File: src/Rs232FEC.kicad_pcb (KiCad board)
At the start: 2 copper layers, 24 x 27.9 mm, 26 parts, among them J1 B5B-XH-A, P1 105444-0001, Q1 DMP3099L-13, U1 FT232RL, U2 MAX232IDR

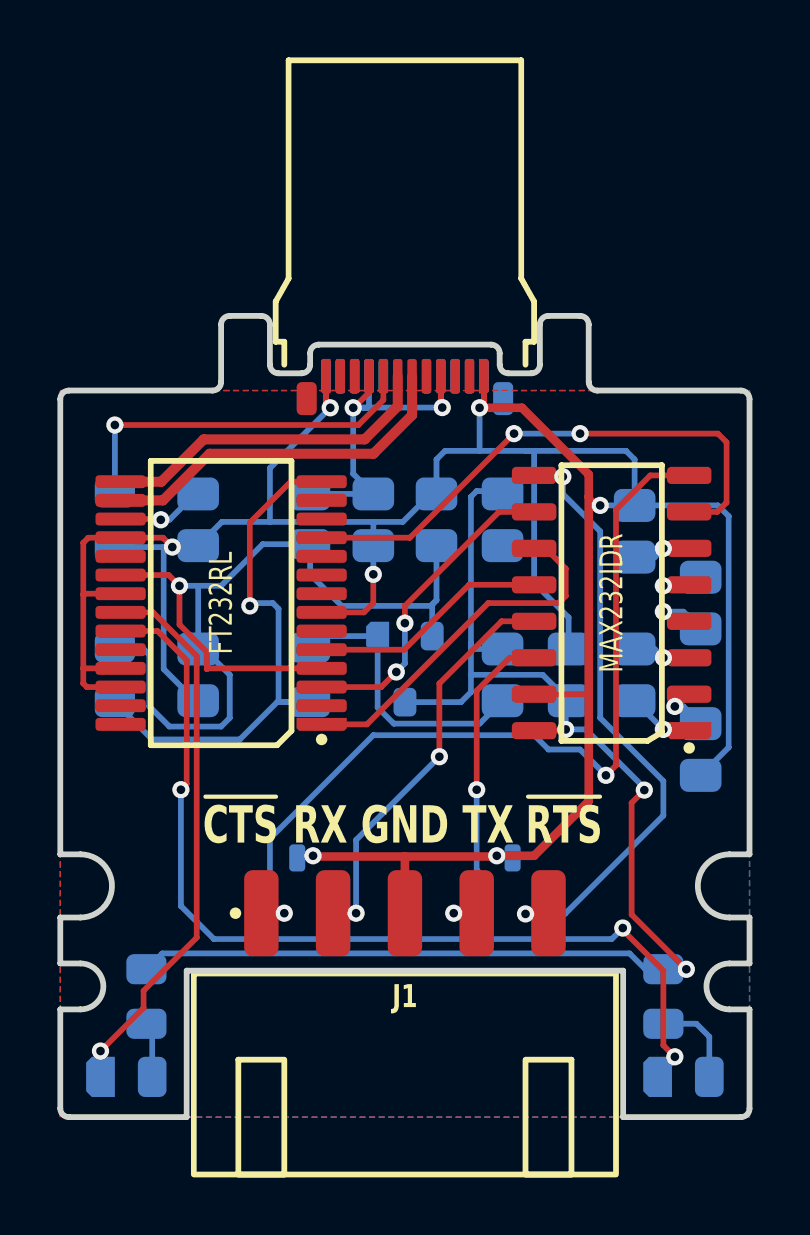
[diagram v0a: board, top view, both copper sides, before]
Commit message: Refactoring copper pour
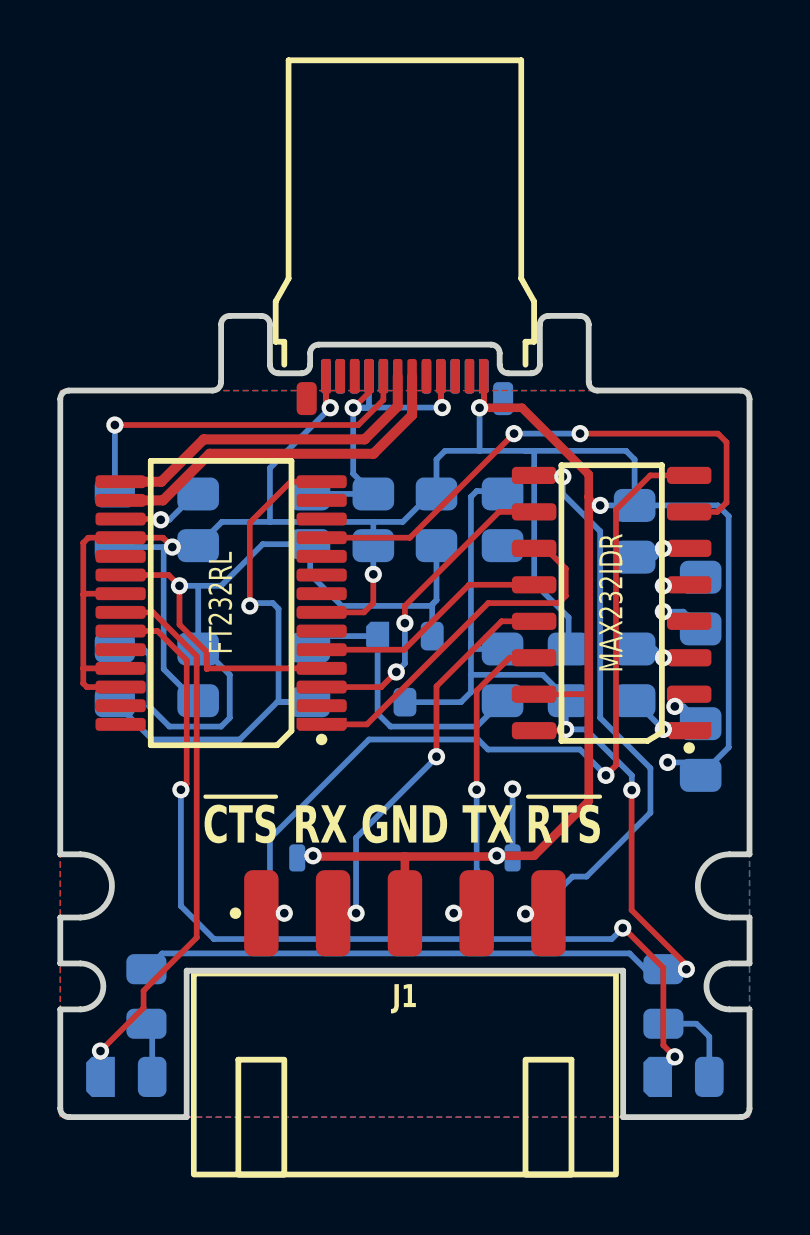
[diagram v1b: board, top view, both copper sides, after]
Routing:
- net GND: track 112.7 -> 116.3 mm, vias 7 -> 9
- net RS232_RTS: track 21.2 -> 20.4 mm
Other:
- rule pad_to_mask_clearance: 0 -> 0.05
